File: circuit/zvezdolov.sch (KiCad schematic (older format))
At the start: 33 parts, among them IC1 ATTINY84A-P, IC2 DM13A, IC3 TLC5943, P1 PWR, P2 ROTENC, P3 ICSP, P4 RGB, Q1 BS170, SW1 SW_RESET, U1 LE33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

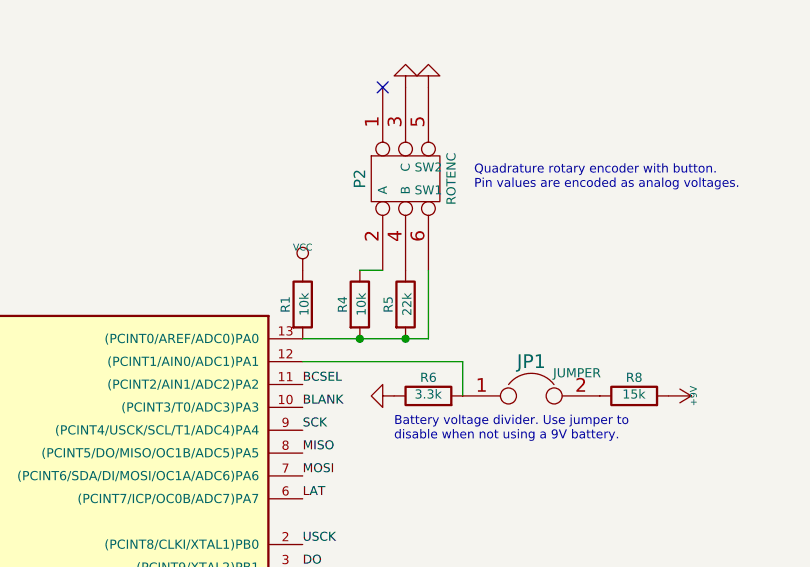
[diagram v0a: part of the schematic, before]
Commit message: Add a debounce capacitor to the encoder.
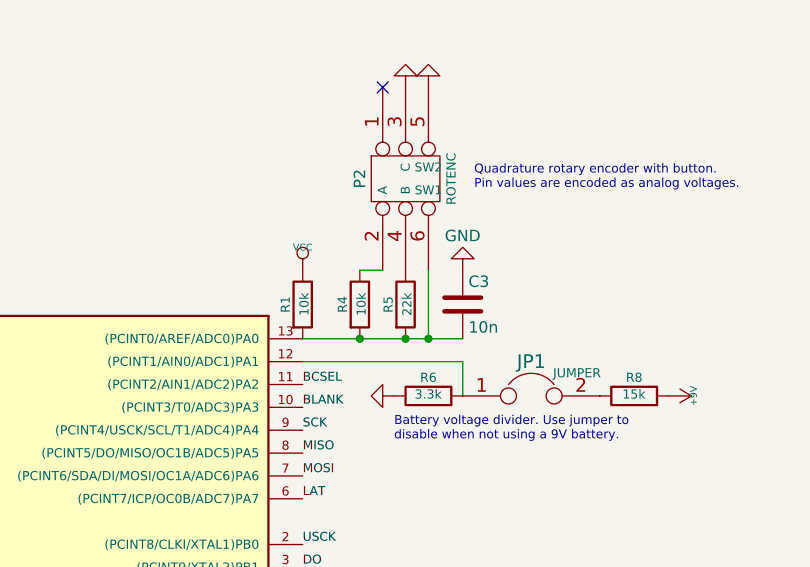
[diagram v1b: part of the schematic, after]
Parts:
- added C3: 10n, Capacitors_ThroughHole:C_Rect_L7_W3.5_P5, symbol C
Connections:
- net GND: now also C3.1
- net at IC1.13 ((PCINT0/AREF/ADC0)PA0), P2.6, R1.2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: now also C3.2
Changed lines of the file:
@@
 	3650 4450 3550 4450
 Wire Wire Line
-	3850 4750 3300 4750
+	3300 4750 4000 4750
 Connection ~ 3550 4750
 Connection ~ 3750 4750
@@
 	-1   0    0    1
 $EndComp
+$Comp
+L C C3
+U 1 1 55868139
+P 4000 4600
+F 0 "C3" H 4025 4700 50  0000 L CNN
+F 1 "10n" H 4025 4500 50  0000 L CNN
+F 2 "Capacitors_ThroughHole:C_Rect_L7_W3.5_P5" H 4038 4450 30  0001 C CNN
+F 3 "" H 4000 4600 60  0000 C CNN
+	1    4000 4600
+	1    0    0    -1
+$EndComp
+Connection ~ 3850 4750
+$Comp
+L GND #PWR041
+U 1 1 5586826F
+P 4000 4450
+F 0 "#PWR041" H 4000 4200 50  0001 C CNN
+F 1 "GND" H 4000 4300 50  0000 C CNN
+F 2 "" H 4000 4450 60  0000 C CNN
+F 3 "" H 4000 4450 60  0000 C CNN
+	1    4000 4450
+	-1   0    0    1
+$EndComp
